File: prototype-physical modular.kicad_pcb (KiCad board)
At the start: 2 copper layers, 100 x 164 mm, 183 parts, among them CON1 BARREL_JACK, CON2 SD_Card_SEEEDOPL, IC1 ATMEGA2560-A, P1 POWER, P10 PC, P11 CONN_UART, P12 PJ, P15 PH, P16 PF, P18 3VI2C, P19 PIGPIO, P20 MIDI_IN, P21 MIDI_OUT, P22 BUSTI, P23 BUSTO, P3 SPI, P7 PA, Q1 BSS138, Q2 BSS138, Q3 BSS138, Q4 BSS138, Q5 BSS138, Q6 BSS138, SW1 SW_PUSH, SW10 SW_PUSH, SW11 SW_PUSH, SW12 SW_PUSH, SW13 SW_PUSH, SW14 SW_PUSH, SW2 ROTARY_ENCODER_SWITCH, SW3 SW_PUSH, SW4 SW_PUSH, SW5 SW_PUSH, SW6 SW_PUSH, SW7 SW_PUSH, SW8 SW_PUSH, SW9 SW_PUSH, U1 NCP1117ST50T3G, U2 6N138, Y1 16MHz

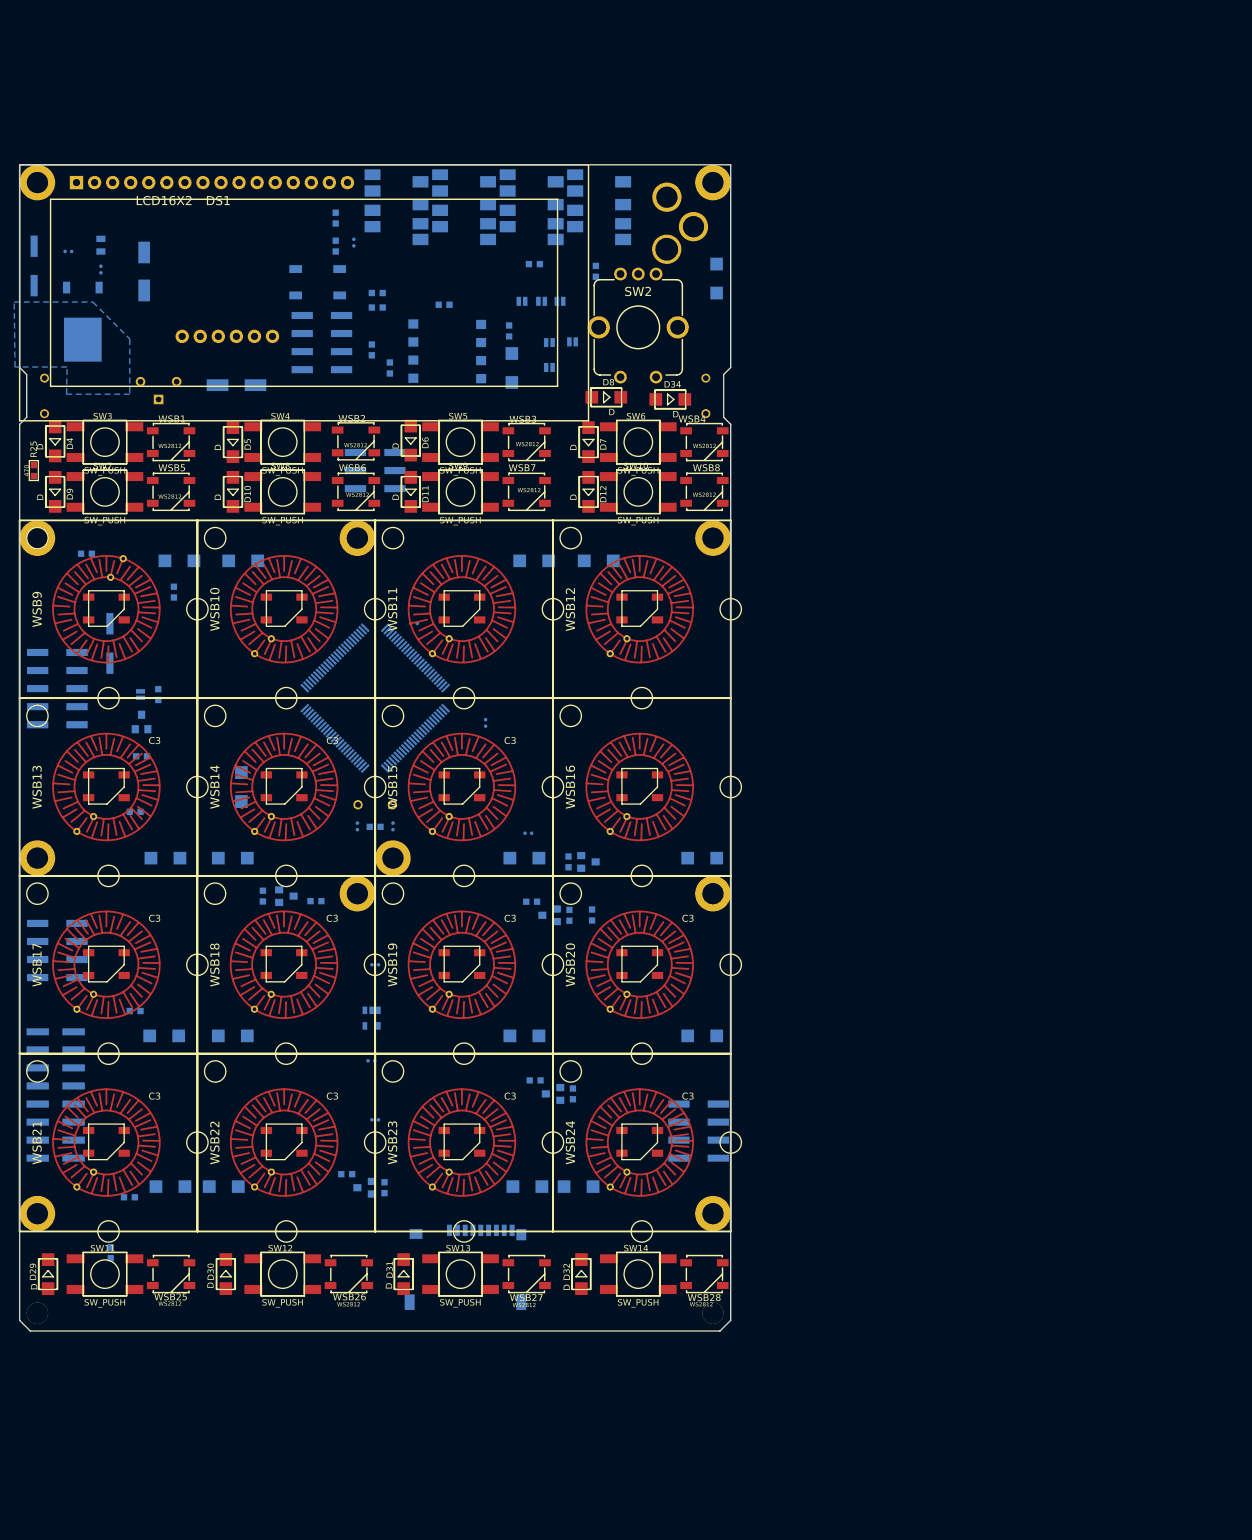
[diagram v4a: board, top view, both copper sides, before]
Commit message: job files for pcb assembly
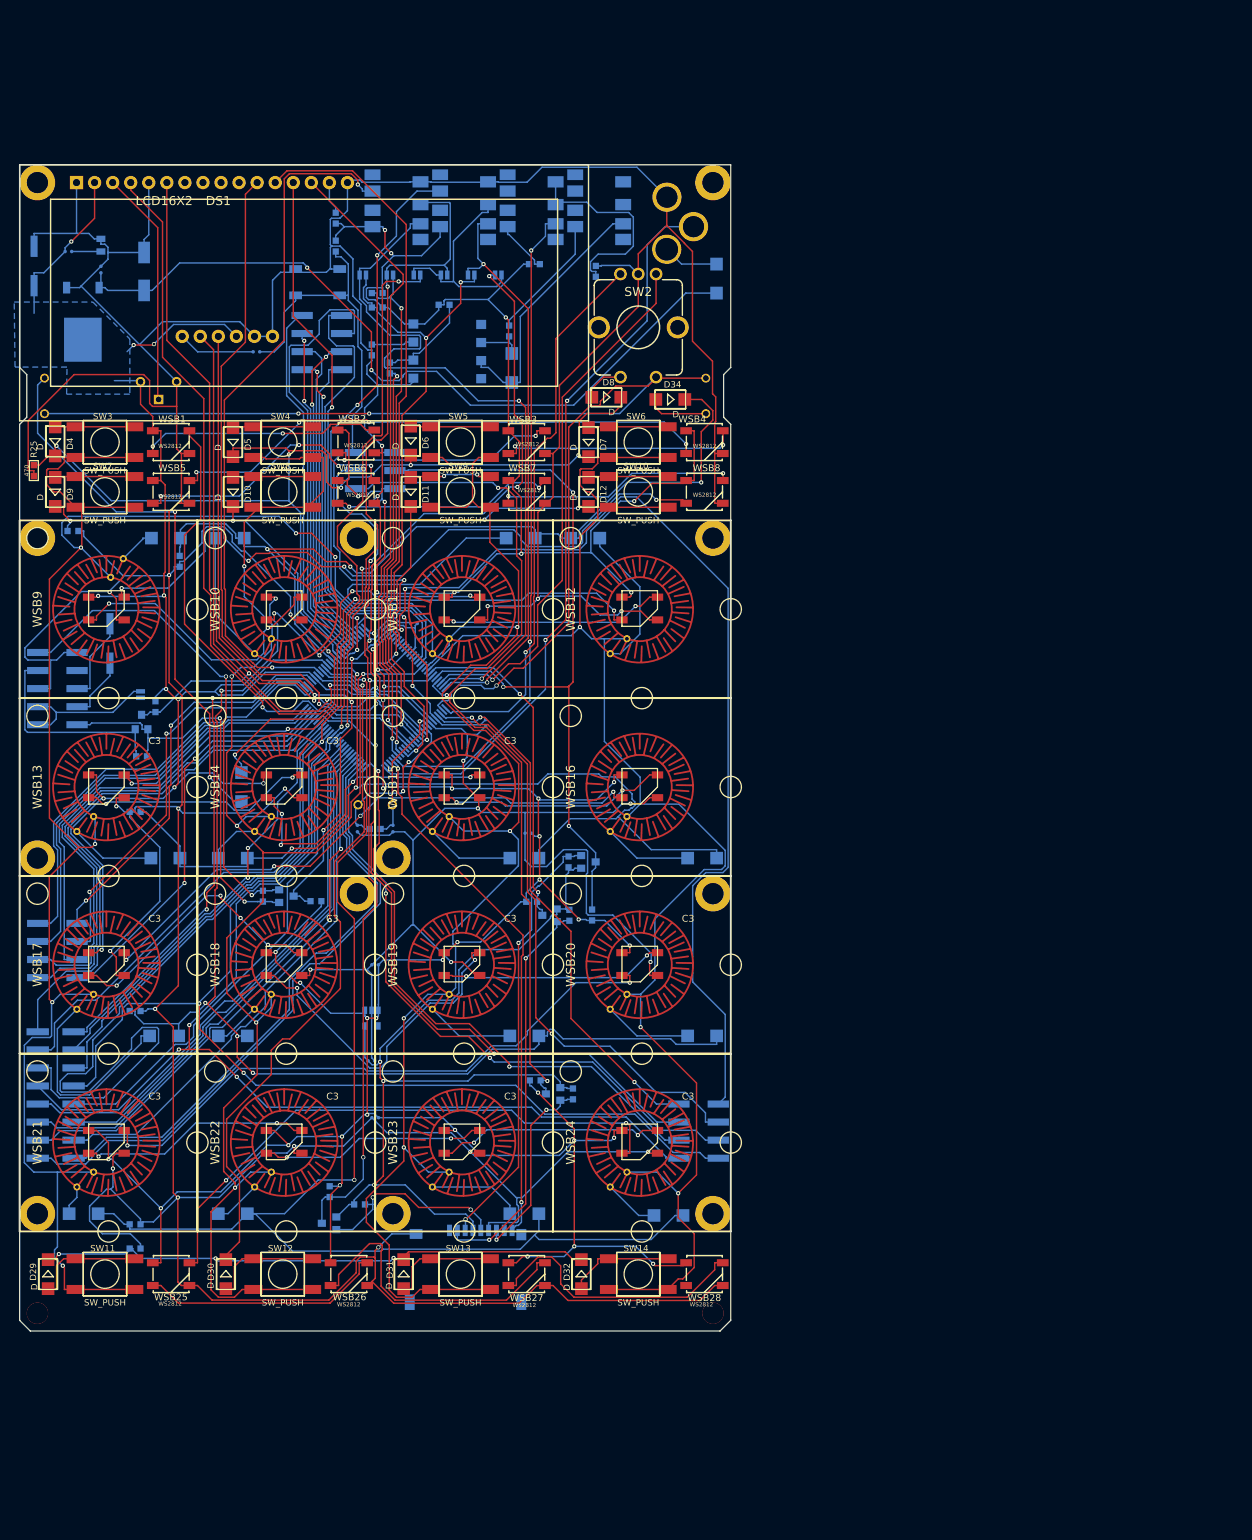
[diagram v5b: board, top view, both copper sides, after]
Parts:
- added H13: hole, lib_fp:hole_with-copper, F.Cu at (52.5, 147.5)
- C1: value 100n -> 100nf
- C11: value Aluminum 47uF-25V -> 100nF; footprint SeeedOPL-Capacitor:ELECTRO-SMD-C-6MM -> SeeedOPL-Capacitor:C0402
- moved C4 36.7 mm to (50.0, 47.5), turned to 90 degrees
- moved JP3 24.2 mm to (52.1, 15.5)
- moved JP4 22.7 mm to (48.3, 15.5)
- moved PJ2COM1 20.9 mm to (55.9, 15.5)
- moved JP1 20.4 mm to (59.7, 15.5)
- moved PJ1COM1 14.9 mm to (67.3, 15.5), turned to 180 degrees
- moved D28 13.3 mm to (91.2, 147.8)
- moved D25 12.8 mm to (9.00, 147.5)
- moved JP5 10.6 mm to (63.5, 15.5)
- moved Q5 7.07 mm to (43.5, 148.8)
- moved C11 5.47 mm to (33.3, 26.3), turned to 270 degrees
- moved R27 4.41 mm to (22.5, 55.8)
- moved R20 4.22 mm to (47.8, 146.2), turned to 270 degrees
- moved D26 4.01 mm to (30.0, 147.5)
- moved R30 3.88 mm to (16.2, 149.0)
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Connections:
- P11 pad 6: Net-(C11-Pad-) -> /DTR
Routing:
- net GND: track 0.00 -> 1134.0 mm, vias 0 -> 27
- net +5V: track 0.00 -> 814.5 mm, vias 0 -> 53
- net /MUXAX0: track 0.00 -> 257.5 mm, vias 0 -> 6
- net /BUS_COM: track 0.00 -> 250.1 mm, vias 0 -> 5
- net /TX3: track 0.00 -> 241.9 mm, vias 0 -> 6
- net /MUXAX1: track 0.00 -> 228.2 mm, vias 0 -> 6
- net /MUXAX3: track 0.00 -> 215.5 mm, vias 0 -> 3
- net /MUXAX2: track 0.00 -> 207.4 mm, vias 0 -> 4
- net Net-(IC1-Pad65): track 0.00 -> 191.4 mm, vias 0 -> 2
- net /MUXBX5: track 0.00 -> 188.8 mm, vias 0 -> 2
- net /MUXBX6: track 0.00 -> 178.4 mm, vias 0 -> 4
- net /MUXAX4: track 0.00 -> 163.3 mm, vias 0 -> 3
- net /MUXBX4: track 0.00 -> 161.9 mm, vias 0 -> 4
- net /MUXBX0: track 0.00 -> 144.8 mm, vias 0 -> 5
- net Net-(IC1-Pad1): track 0.00 -> 144.5 mm, vias 0 -> 2
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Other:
- net class power: trace_width 0.3 -> 0.2032
- board text added: "DTR"
- board text added: "RX"
- board text added: "TX"

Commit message: add slot for capacitor in case reset doesn't work
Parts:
- added H17: hole, lib_fp:hole_with-copper, F.Cu at (102.6, 174.1)
- added H19: hole, lib_fp:hole_with-copper, F.Cu at (128.9, 174.1)
- added H25: hole, lib_fp:hole_no-copper, F.Cu at (142.0, 174.1)
- added P13: PD, Pin_Headers:Pin_Header_Straight_2x04_Pitch2.54mm_SMD, F.Cu at (89.4, 174.1)
- added P14: PE, Pin_Headers:Pin_Header_Straight_2x04_Pitch2.54mm_SMD, F.Cu at (50.0, 174.1)
- added P17: SD_PINS, Pin_Headers:Pin_Header_Straight_1x10_Pitch2.54mm_SMD_Pin1Left, F.Cu at (168.3, 178.6)
- added P2: FTDI, Pin_Headers:Pin_Header_Straight_1x06_Pitch2.54mm_SMD_Pin1Left, F.Cu at (115.7, 174.1)
- added P8: PL, Pin_Headers:Pin_Header_Straight_2x04_Pitch2.54mm_SMD, F.Cu at (63.1, 174.1)
- added P9: PB, Pin_Headers:Pin_Header_Straight_2x04_Pitch2.54mm_SMD, F.Cu at (76.3, 174.1)
- added PCap1: CONN_01X02, SparkFun-Connectors:1X02, B.Cu at (34.3, 29.1)
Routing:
- net /DTR: track 11.6 -> 14.9 mm
- net /RESET: track 108.0 -> 111.0 mm

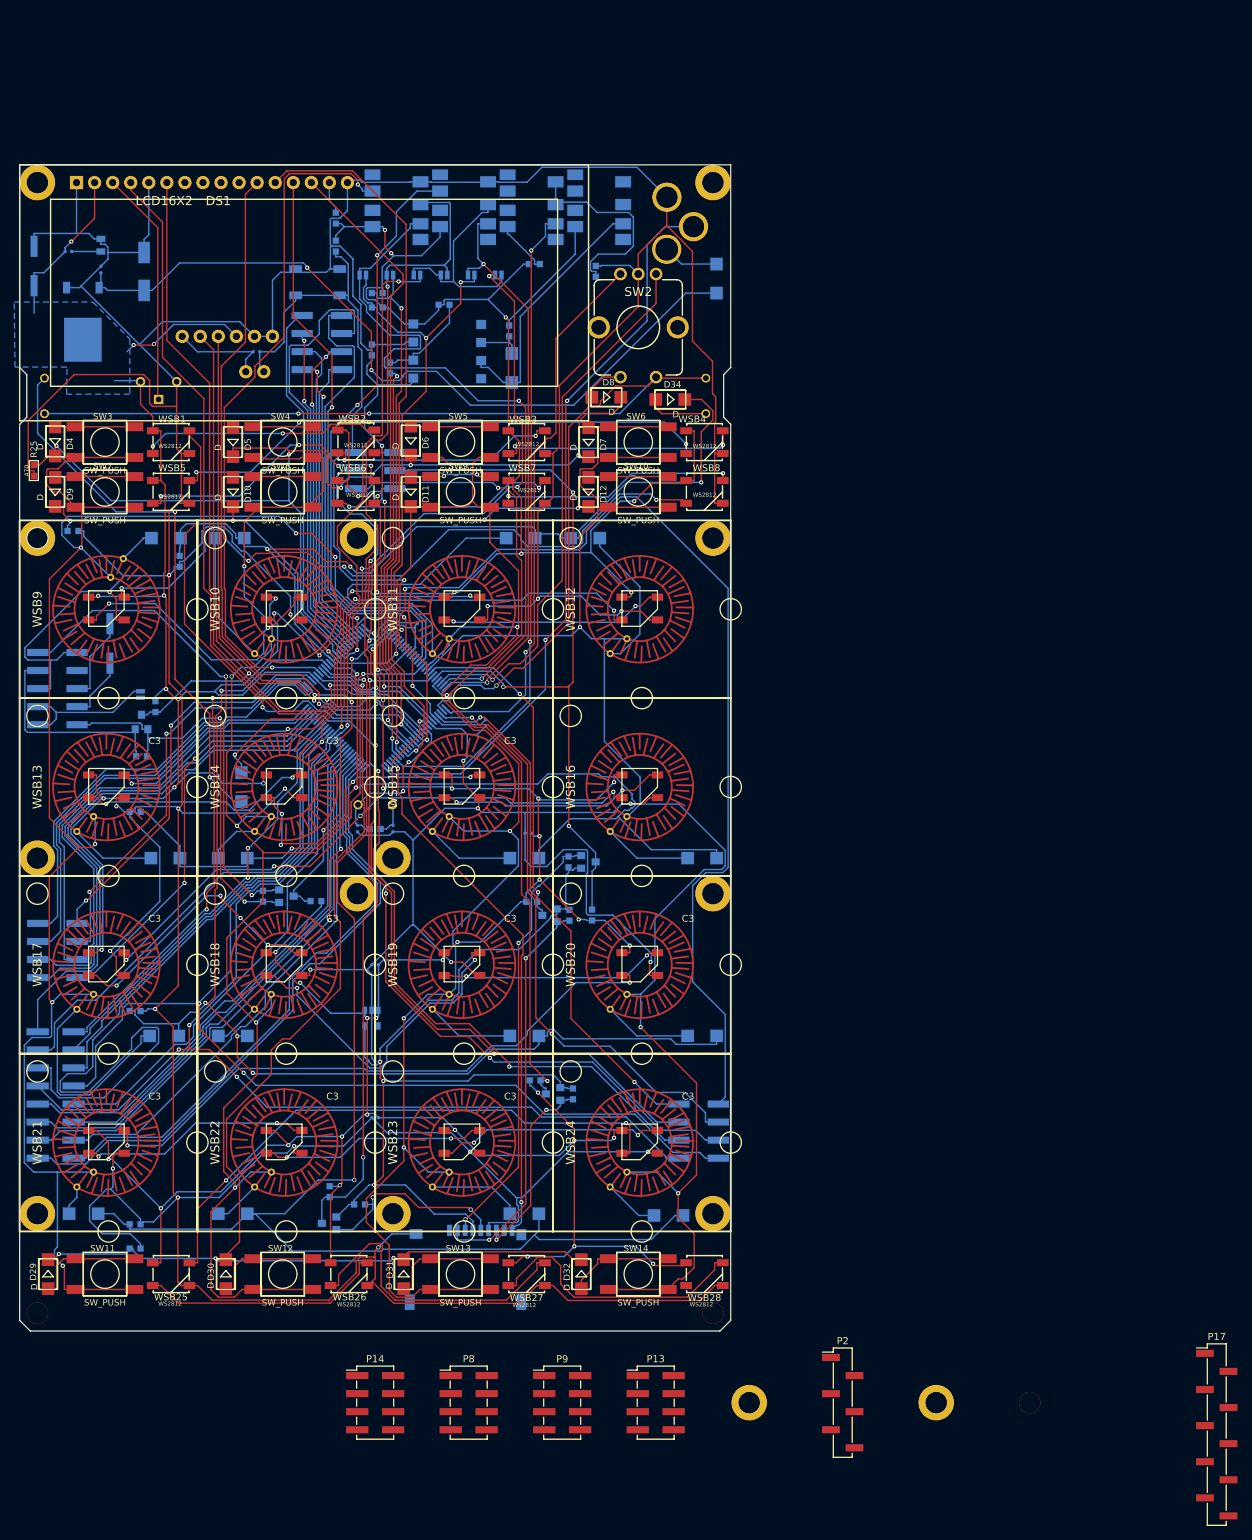
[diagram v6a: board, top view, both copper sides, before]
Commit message: manual route effort that will not be used
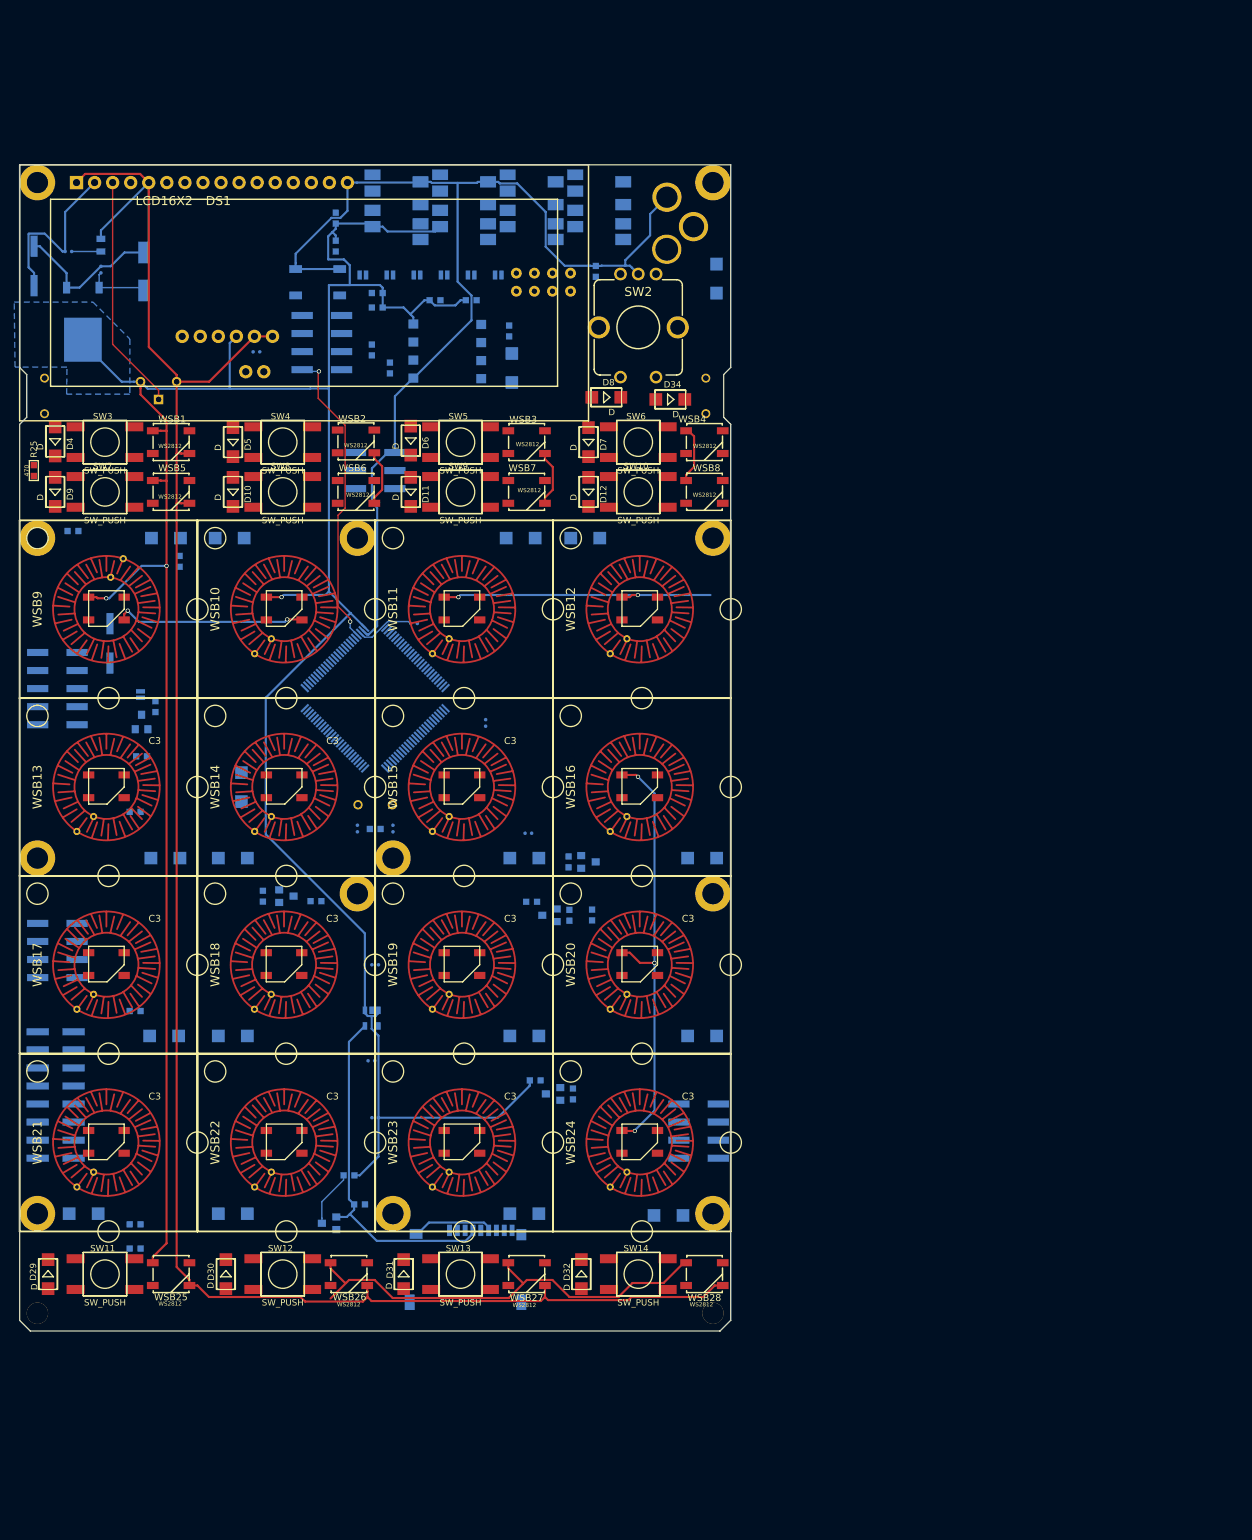
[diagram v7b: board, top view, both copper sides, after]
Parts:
- removed H17, H19: hole, lib_fp:hole_with-copper
- removed H25: hole, lib_fp:hole_no-copper
- removed P13: PD, Pin_Headers:Pin_Header_Straight_2x04_Pitch2.54mm_SMD
- removed P14: PE, Pin_Headers:Pin_Header_Straight_2x04_Pitch2.54mm_SMD
- removed P17: SD_PINS, Pin_Headers:Pin_Header_Straight_1x10_Pitch2.54mm_SMD_Pin1Left
- removed P2: FTDI, Pin_Headers:Pin_Header_Straight_1x06_Pitch2.54mm_SMD_Pin1Left
- removed P8: PL, Pin_Headers:Pin_Header_Straight_2x04_Pitch2.54mm_SMD
- removed P9: PB, Pin_Headers:Pin_Header_Straight_2x04_Pitch2.54mm_SMD
- added P4: CONN_02X02, lib_fp:xjump, B.Cu at (71.1, 16.5)
- added P5: CONN_02X02, lib_fp:xjump, B.Cu at (76.2, 16.5)
- moved R2 10.2 mm to (63.5, 19.1)
- moved R19 3.56 mm to (46.3, 142.1), turned to 270 degrees
- moved R6 1.42 mm to (58.4, 19.1)
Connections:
- D3 pad +: Net-(D3-Pad+) -> /MIDI_IN_RX_PRE
- P20 pad 3: Net-(D3-Pad+) -> Net-(P20-Pad3)
- P21 pad 3: /MIDI_OUT_TX -> Net-(P21-Pad3)
- R2 pad 2: Net-(P21-Pad4) -> Net-(P4-Pad2)
- R4 pad 1: Net-(P20-Pad4) -> Net-(P5-Pad2)
- U2 pad 3: Net-(D3-Pad+) -> /MIDI_IN_RX_PRE
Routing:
- net GND: track 1134.0 -> 522.3 mm, vias 27 -> 2
- net /MUXAX0: track 257.5 -> 0.00 mm, vias 6 -> 0
- net /BUS_COM: track 250.1 -> 0.00 mm, vias 5 -> 0
- net /TX3: track 241.9 -> 0.00 mm, vias 6 -> 0
- net /MUXAX1: track 228.2 -> 0.00 mm, vias 6 -> 0
- net /MUXAX3: track 215.5 -> 0.00 mm, vias 3 -> 0
- net /MUXAX2: track 207.4 -> 0.00 mm, vias 4 -> 0
- net +5V: track 814.5 -> 621.5 mm, vias 53 -> 8
- net Net-(IC1-Pad65): track 191.4 -> 0.00 mm, vias 2 -> 0
- net /MUXBX5: track 188.8 -> 0.00 mm, vias 2 -> 0
- net /MUXBX6: track 178.4 -> 0.00 mm, vias 4 -> 0
- net /MUXAX4: track 163.3 -> 0.00 mm, vias 3 -> 0
- net /MUXBX4: track 161.9 -> 0.00 mm, vias 4 -> 0
- net /MUXBX0: track 144.8 -> 0.00 mm, vias 5 -> 0
- net Net-(IC1-Pad1): track 144.5 -> 0.00 mm, vias 2 -> 0
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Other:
- net class power: trace_width 0.2032 -> 0.3

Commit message: enclosure changes and new prints. Unknown changes
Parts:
- added +5V: >VALUE, SparkFun-Connectors:1X01, F.Cu at (22.9, 21.3)
- moved JP4 6.29 mm to (54.0, 18.0), turned to 90 degrees
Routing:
- net GND: track 522.3 -> 1010.6 mm, vias 2 -> 27
- net /BUS_COM: track 0.00 -> 264.8 mm, vias 0 -> 3
- net /MUXAX0: track 0.00 -> 240.4 mm, vias 0 -> 5
- net /TX3: track 0.00 -> 223.5 mm, vias 0 -> 5
- net /MUXAX1: track 0.00 -> 210.6 mm, vias 0 -> 6
- net /MUXAX3: track 0.00 -> 209.3 mm, vias 0 -> 4
- net /MUXBX6: track 0.00 -> 207.2 mm, vias 0 -> 4
- net /MUXAX2: track 0.00 -> 197.9 mm, vias 0 -> 4
- net /MUXBX5: track 0.00 -> 186.0 mm, vias 0 -> 2
- net /MUXAX4: track 0.00 -> 179.1 mm, vias 0 -> 1
- net +5V: track 621.5 -> 791.6 mm, vias 8 -> 54
- net Net-(IC1-Pad65): track 0.00 -> 153.8 mm, vias 0 -> 2
- net /MUXBX1: track 0.00 -> 149.0 mm, vias 0 -> 6
- net /MUXBX4: track 0.00 -> 148.0 mm, vias 0 -> 3
- net /MUXBX3: track 0.00 -> 134.1 mm, vias 0 -> 5
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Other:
- net class Default: clearance 0.127 -> 0.1524; trace_width 0.2 -> 0.1524
- net class power: clearance 0.127 -> 0.1524
- rule trace_clearance: 0.127 -> 0.1524
- board text added: "AUTOTEL.CO calculeitor 10.11.2017"
- board text added: "Error"
- board text added: "hole, jump"
- board text added: "https://www.hammfg.com/files/parts/pdf/1455L1601.pdf"
- board text added: "ready checklist: - DRC - No wires on the press pad areas -"
- board text added: "switch positions of I/O ?"
- board text removed: "AUTOTEL.CO calculator 10.11.2017"
